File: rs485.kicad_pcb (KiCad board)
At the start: 2 copper layers, 22.2 x 20.3 mm, 17 parts, among them J1 Screw_Terminal_1x02, J2 Screw_Terminal_1x02, J3 CONN_01X03, J4 CONN_01X06, U1 MAX485E

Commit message: Added to silkscreen: +5V, GND
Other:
- board text added: "+5V"
- board text added: "GND"
- board text added: "V1.1"
- board text removed: "V1.0"
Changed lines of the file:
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@@
     (area 130.734999 84.379999 153.110001 104.850001)
     (thickness 1.6)
-    (drawings 16)
+    (drawings 18)
     (tracks 156)
     (zones 0)
@@
   (page A4)
   (layers
-    (0 F.Cu signal)
+    (0 F.Cu signal hide)
     (31 B.Cu signal)
     (32 B.Adhes user)
@@
       (net 12 "Net-(J4-Pad4)"))
   )
+  (gr_text GND (at 151.257 89.662 90) (layer B.SilkS)
+    (effects (font (size 1.5 1.5) (thickness 0.3)) (justify mirror))
+  )
+  (gr_text +5V (at 151.257 95.631 90) (layer B.SilkS)
+    (effects (font (size 1.5 1.5) (thickness 0.3)) (justify mirror))
+  )
   (gr_text 2017-08-27 (at 213.868 193.04) (layer Dwgs.User)
     (effects (font (size 1.5 1.5) (thickness 0.3)))
@@
     (effects (font (size 1.5 1.5) (thickness 0.3)))
   )
-  (gr_text V1.0 (at 270.891 193.167) (layer Dwgs.User)
+  (gr_text V1.1 (at 270.891 193.167) (layer Dwgs.User)
     (effects (font (size 1.5 1.5) (thickness 0.3)))
   )

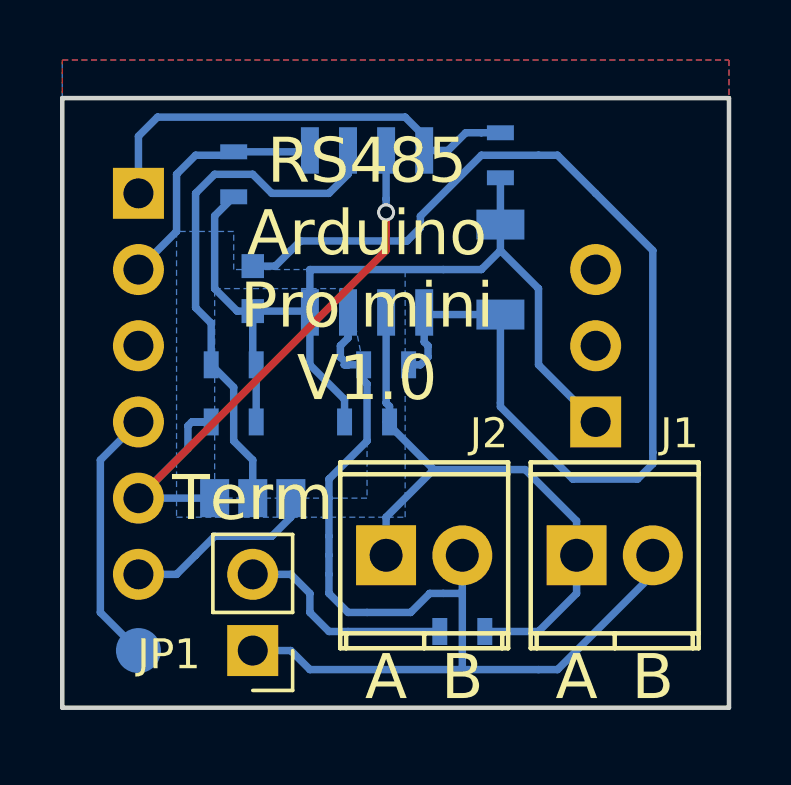
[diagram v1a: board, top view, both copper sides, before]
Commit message: Added OSHW logo, pin descriptions, changed version
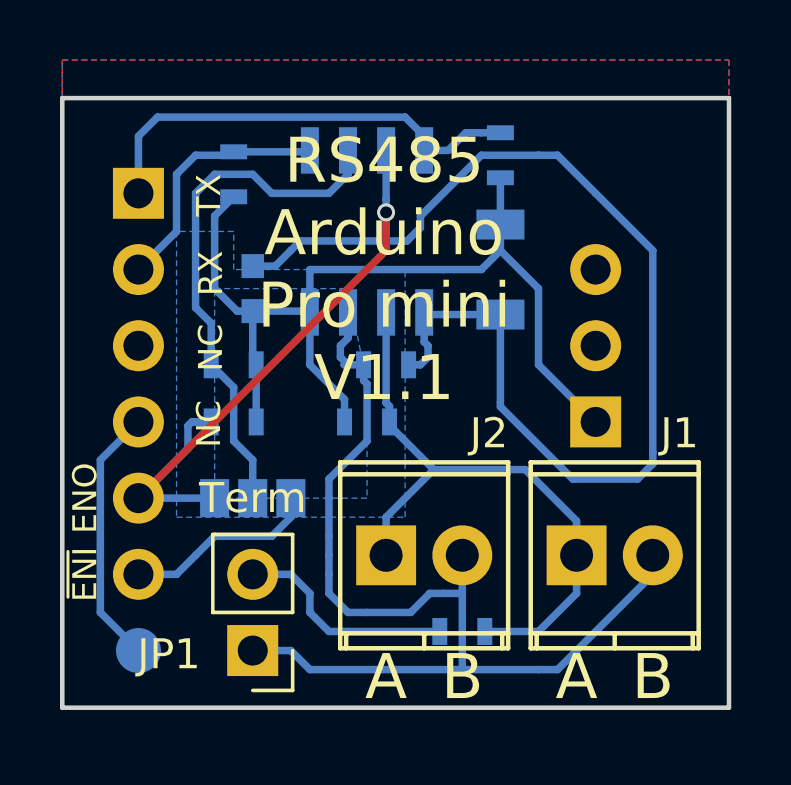
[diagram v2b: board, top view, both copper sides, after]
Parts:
- added REF***: OSHW-Logo2_7.3x6mm_SilkScreen, Symbols:OSHW-Logo2_7.3x6mm_SilkScreen, B.Cu at (144.8, 95.6)
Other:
- board text added: "ENI"
- board text added: "ENO"
- board text added: "NC"
- board text added: "RS485 Arduino Pro mini V1.1"
- board text added: "RX"
- board text added: "TX"
- board text removed: "RS485 Arduino Pro mini V1.0"
